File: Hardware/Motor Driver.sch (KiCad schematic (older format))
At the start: 9 parts, among them U5 DRV8874

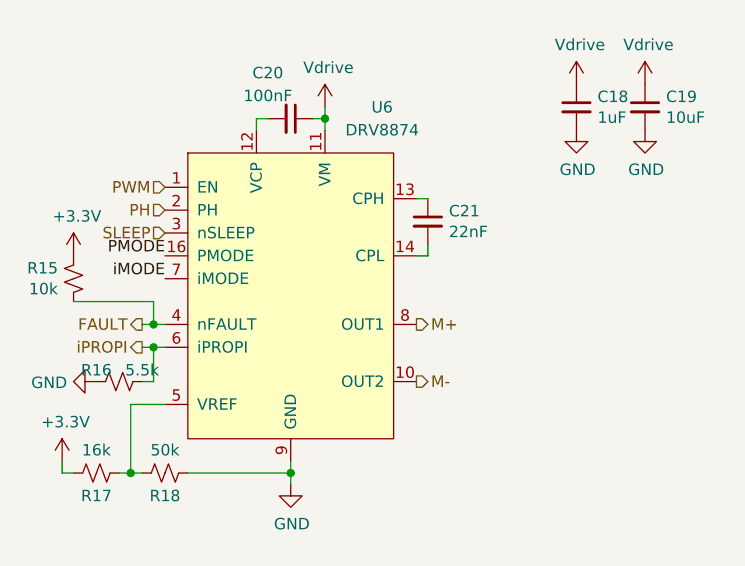
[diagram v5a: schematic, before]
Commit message: Replaced ESP-WROOM-32D with ESP32-CAM
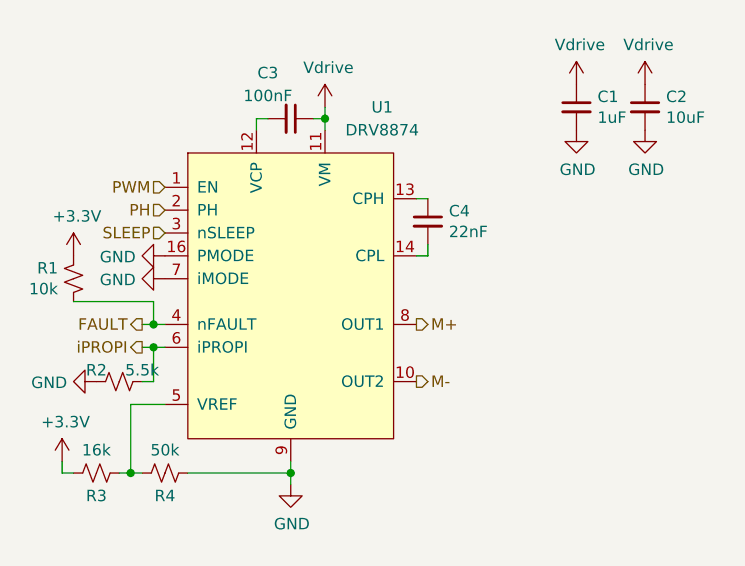
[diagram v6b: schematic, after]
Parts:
- renumbered C14 to C1, C15 to C2, C16 to C3, C17 to C4, R11 to R1, R12 to R2, R13 to R3, R14 to R4, U5 to U1
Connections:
- net PMODE is gone; now on net GND: U1.16 (PMODE)
- net iMODE is gone; now on net GND: U1.7 (iMODE)
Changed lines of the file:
@@
 P 5850 4500
 AR Path="/5FF172EF" Ref="#PWR?"  Part="1"
-AR Path="/5FF00151/5FF172EF" Ref="#PWR027"  Part="1"
-AR Path="/5FF2CF13/5FF172EF" Ref="#PWR036"  Part="1"
-F 0 "#PWR036" H 5850 4250 50  0001 C CNN
+AR Path="/5FF00151/5FF172EF" Ref="#PWR014"  Part="1"
+AR Path="/5FF2CF13/5FF172EF" Ref="#PWR025"  Part="1"
+F 0 "#PWR025" H 5850 4250 50  0001 C CNN
 F 1 "GND" H 5855 4327 50  0000 C CNN
 F 2 "" H 5850 4500 50  0001 C CNN
@@
 AR Path="/5EA2026E/5FF2BF81" Ref="C?"  Part="1"
 AR Path="/5FF2BF81" Ref="C?"  Part="1"
-AR Path="/5FF00151/5FF2BF81" Ref="C17"  Part="1"
-AR Path="/5FF2CF13/5FF2BF81" Ref="C21"  Part="1"
-F 0 "C21" H 6542 3396 50  0000 L CNN
+AR Path="/5FF00151/5FF2BF81" Ref="C4"  Part="1"
+AR Path="/5FF2CF13/5FF2BF81" Ref="C8"  Part="1"
+F 0 "C4" H 6542 3396 50  0000 L CNN
 F 1 "22nF" H 6542 3305 50  0000 L CNN
 F 2 "Resistor_SMD:R_0603_1608Metric" H 6450 3350 50  0001 C CNN
@@
 P 4850 4400
 AR Path="/5FF2D4A0" Ref="#PWR?"  Part="1"
-AR Path="/5FF00151/5FF2D4A0" Ref="#PWR026"  Part="1"
-AR Path="/5FF2CF13/5FF2D4A0" Ref="#PWR035"  Part="1"
-F 0 "#PWR035" H 4850 4250 50  0001 C CNN
+AR Path="/5FF00151/5FF2D4A0" Ref="#PWR013"  Part="1"
+AR Path="/5FF2CF13/5FF2D4A0" Ref="#PWR024"  Part="1"
+F 0 "#PWR024" H 4850 4250 50  0001 C CNN
 F 1 "+3.3V" H 4865 4573 50  0000 C CNN
 F 2 "" H 4850 4400 50  0001 C CNN
@@
 P 5000 4450
 AR Path="/5FF172DB" Ref="R?"  Part="1"
-AR Path="/5FF00151/5FF172DB" Ref="R13"  Part="1"
-AR Path="/5FF2CF13/5FF172DB" Ref="R17"  Part="1"
-F 0 "R17" V 5100 4450 50  0000 C CNN
+AR Path="/5FF00151/5FF172DB" Ref="R3"  Part="1"
+AR Path="/5FF2CF13/5FF172DB" Ref="R7"  Part="1"
+F 0 "R3" V 5100 4450 50  0000 C CNN
 F 1 "16k" V 4900 4450 50  0000 C CNN
 F 2 "Resistor_SMD:R_0603_1608Metric" H 5000 4450 50  0001 C CNN
@@
 P 7400 2750
 AR Path="/5FF2D498" Ref="#PWR?"  Part="1"
-AR Path="/5FF00151/5FF2D498" Ref="#PWR020"  Part="1"
-AR Path="/5FF2CF13/5FF2D498" Ref="#PWR029"  Part="1"
-F 0 "#PWR029" H 7200 2600 50  0001 C CNN
+AR Path="/5FF00151/5FF2D498" Ref="#PWR05"  Part="1"
+AR Path="/5FF2CF13/5FF2D498" Ref="#PWR016"  Part="1"
+F 0 "#PWR016" H 7200 2600 50  0001 C CNN
 F 1 "Vdrive" H 7415 2923 50  0000 C CNN
 F 2 "" H 7400 2750 50  0001 C CNN
@@
 P 7100 2750
 AR Path="/5FF172EC" Ref="#PWR?"  Part="1"
-AR Path="/5FF00151/5FF172EC" Ref="#PWR019"  Part="1"
-AR Path="/5FF2CF13/5FF172EC" Ref="#PWR028"  Part="1"
-F 0 "#PWR028" H 6900 2600 50  0001 C CNN
+AR Path="/5FF00151/5FF172EC" Ref="#PWR04"  Part="1"
+AR Path="/5FF2CF13/5FF172EC" Ref="#PWR015"  Part="1"
+F 0 "#PWR015" H 6900 2600 50  0001 C CNN
 F 1 "Vdrive" H 7115 2923 50  0000 C CNN
 F 2 "" H 7100 2750 50  0001 C CNN
@@
 P 7100 2850
 AR Path="/5FF172D6" Ref="C?"  Part="1"
-AR Path="/5FF00151/5FF172D6" Ref="C14"  Part="1"
-AR Path="/5FF2CF13/5FF172D6" Ref="C18"  Part="1"
-F 0 "C18" H 7192 2896 50  0000 L CNN
+AR Path="/5FF00151/5FF172D6" Ref="C1"  Part="1"
+AR Path="/5FF2CF13/5FF172D6" Ref="C5"  Part="1"
+F 0 "C1" H 7192 2896 50  0000 L CNN
 F 1 "1uF" H 7192 2805 50  0000 L CNN
 F 2 "Resistor_SMD:R_0603_1608Metric" H 7100 2850 50  0001 C CNN
@@
 P 7100 2950
 AR Path="/5FF2BF19" Ref="#PWR?"  Part="1"
-AR Path="/5FF00151/5FF2BF19" Ref="#PWR022"  Part="1"
-AR Path="/5FF2CF13/5FF2BF19" Ref="#PWR031"  Part="1"
-F 0 "#PWR031" H 7100 2700 50  0001 C CNN
+AR Path="/5FF00151/5FF2BF19" Ref="#PWR07"  Part="1"
+AR Path="/5FF2CF13/5FF2BF19" Ref="#PWR018"  Part="1"
+F 0 "#PWR018" H 7100 2700 50  0001 C CNN
 F 1 "GND" H 7105 2777 50  0000 C CNN
 F 2 "" H 7100 2950 50  0001 C CNN
@@
 P 7400 2950
 AR Path="/5FF2D48C" Ref="#PWR?"  Part="1"
-AR Path="/5FF00151/5FF2D48C" Ref="#PWR023"  Part="1"
-AR Path="/5FF2CF13/5FF2D48C" Ref="#PWR032"  Part="1"
-F 0 "#PWR032" H 7400 2700 50  0001 C CNN
+AR Path="/5FF00151/5FF2D48C" Ref="#PWR08"  Part="1"
+AR Path="/5FF2CF13/5FF2D48C" Ref="#PWR019"  Part="1"
+F 0 "#PWR019" H 7400 2700 50  0001 C CNN
 F 1 "GND" H 7405 2777 50  0000 C CNN
 F 2 "" H 7400 2950 50  0001 C CNN
@@
 P 5000 4050
 AR Path="/5FF2D49F" Ref="#PWR?"  Part="1"
-AR Path="/5FF00151/5FF2D49F" Ref="#PWR025"  Part="1"
-AR Path="/5FF2CF13/5FF2D49F" Ref="#PWR034"  Part="1"
-F 0 "#PWR034" H 5000 3800 50  0001 C CNN
+AR Path="/5FF00151/5FF2D49F" Ref="#PWR012"  Part="1"
+AR Path="/5FF2CF13/5FF2D49F" Ref="#PWR023"  Part="1"
+F 0 "#PWR023" H 5000 3800 50  0001 C CNN
 F 1 "GND" V 5005 3922 50  0000 R CNN
 F 2 "" H 5000 4050 50  0001 C CNN
@@
 AR Path="/5EA2026E/5FF2D494" Ref="R?"  Part="1"
 AR Path="/5FF2D494" Ref="R?"  Part="1"
-AR Path="/5FF00151/5FF2D494" Ref="R11"  Part="1"
-AR Path="/5FF2CF13/5FF2D494" Ref="R15"  Part="1"
-F 0 "R15" H 4968 3646 50  0000 L CNN
+AR Path="/5FF00151/5FF2D494" Ref="R1"  Part="1"
+AR Path="/5FF2CF13/5FF2D494" Ref="R5"  Part="1"
+F 0 "R1" H 4968 3646 50  0000 L CNN
 F 1 "10k" H 4968 3555 50  0000 L CNN
 F 2 "Resistor_SMD:R_0603_1608Metric" H 4900 3600 50  0001 C CNN
@@
 Text HLabel 5300 3400 0    50   Input ~ 0
 SLEEP
-Text Label 5300 3500 2    50   ~ 0
-PMODE
-Text Label 5300 3600 2    50   ~ 0
-iMODE
 Text HLabel 5200 3800 0    50   Output ~ 0
 FAULT
@@
 P 7400 2850
 AR Path="/5FF2D490" Ref="C?"  Part="1"
-AR Path="/5FF00151/5FF2D490" Ref="C15"  Part="1"
-AR Path="/5FF2CF13/5FF2D490" Ref="C19"  Part="1"
-F 0 "C19" H 7492 2896 50  0000 L CNN
+AR Path="/5FF00151/5FF2D490" Ref="C2"  Part="1"
+AR Path="/5FF2CF13/5FF2D490" Ref="C6"  Part="1"
+F 0 "C2" H 7492 2896 50  0000 L CNN
 F 1 "10uF" H 7492 2805 50  0000 L CNN
 F 2 "Capacitor_SMD:C_2220_5650Metric" H 7400 2850 50  0001 C CNN
@@
 P 4900 3500
 AR Path="/5FF172E1" Ref="#PWR?"  Part="1"
-AR Path="/5FF00151/5FF172E1" Ref="#PWR024"  Part="1"
-AR Path="/5FF2CF13/5FF172E1" Ref="#PWR033"  Part="1"
-F 0 "#PWR033" H 4900 3350 50  0001 C CNN
+AR Path="/5FF00151/5FF172E1" Ref="#PWR09"  Part="1"
+AR Path="/5FF2CF13/5FF172E1" Ref="#PWR020"  Part="1"
+F 0 "#PWR020" H 4900 3350 50  0001 C CNN
 F 1 "+3.3V" H 4915 3673 50  0000 C CNN
 F 2 "" H 4900 3500 50  0001 C CNN
@@
 P 5100 4050
 AR Path="/5FF2D49E" Ref="R?"  Part="1"
-AR Path="/5FF00151/5FF2D49E" Ref="R12"  Part="1"
-AR Path="/5FF2CF13/5FF2D49E" Ref="R16"  Part="1"
-F 0 "R16" V 5050 3950 50  0000 C CNN
+AR Path="/5FF00151/5FF2D49E" Ref="R2"  Part="1"
+AR Path="/5FF2CF13/5FF2D49E" Ref="R6"  Part="1"
+F 0 "R2" V 5050 3950 50  0000 C CNN
 F 1 "5.5k" V 5050 4150 50  0000 C CNN
 F 2 "Resistor_SMD:R_0603_1608Metric" H 5100 4050 50  0001 C CNN
@@
 P 5300 4450
 AR Path="/5FF172DD" Ref="R?"  Part="1"
-AR Path="/5FF00151/5FF172DD" Ref="R14"  Part="1"
-AR Path="/5FF2CF13/5FF172DD" Ref="R18"  Part="1"
-F 0 "R18" V 5400 4450 50  0000 C CNN
+AR Path="/5FF00151/5FF172DD" Ref="R4"  Part="1"
+AR Path="/5FF2CF13/5FF172DD" Ref="R8"  Part="1"
+F 0 "R4" V 5400 4450 50  0000 C CNN
 F 1 "50k" V 5200 4450 50  0000 C CNN
 F 2 "Resistor_SMD:R_0603_1608Metric" H 5300 4450 50  0001 C CNN
@@
 P 6000 2850
 AR Path="/5FF2D4A1" Ref="#PWR?"  Part="1"
-AR Path="/5FF00151/5FF2D4A1" Ref="#PWR021"  Part="1"
-AR Path="/5FF2CF13/5FF2D4A1" Ref="#PWR030"  Part="1"
-F 0 "#PWR030" H 5800 2700 50  0001 C CNN
+AR Path="/5FF00151/5FF2D4A1" Ref="#PWR06"  Part="1"
+AR Path="/5FF2CF13/5FF2D4A1" Ref="#PWR017"  Part="1"
+F 0 "#PWR017" H 5800 2700 50  0001 C CNN
 F 1 "Vdrive" H 6015 3023 50  0000 C CNN
 F 2 "" H 6000 2850 50  0001 C CNN
@@
 P 5850 2900
 AR Path="/5FF2D4A2" Ref="C?"  Part="1"
-AR Path="/5FF00151/5FF2D4A2" Ref="C16"  Part="1"
-AR Path="/5FF2CF13/5FF2D4A2" Ref="C20"  Part="1"
-F 0 "C20" V 5650 2800 50  0000 C CNN
+AR Path="/5FF00151/5FF2D4A2" Ref="C3"  Part="1"
+AR Path="/5FF2CF13/5FF2D4A2" Ref="C7"  Part="1"
+F 0 "C3" V 5650 2800 50  0000 C CNN
 F 1 "100nF" V 5750 2800 50  0000 C CNN
 F 2 "Resistor_SMD:R_0603_1608Metric" H 5850 2900 50  0001 C CNN
@@
 P 5850 3050
 AR Path="/5FF172F1" Ref="U?"  Part="1"
-AR Path="/5FF00151/5FF172F1" Ref="U5"  Part="1"
-AR Path="/5FF2CF13/5FF172F1" Ref="U6"  Part="1"
-F 0 "U6" H 6250 3250 50  0000 C CNN
+AR Path="/5FF00151/5FF172F1" Ref="U1"  Part="1"
+AR Path="/5FF2CF13/5FF172F1" Ref="U2"  Part="1"
+F 0 "U1" H 6250 3250 50  0000 C CNN
 F 1 "DRV8874" H 6250 3150 50  0000 C CNN
 F 2 "Package_SO:HTSSOP-16-1EP_4.4x5mm_P0.65mm_EP3.4x5mm_Mask3x3mm_ThermalVias" H 6200 3200 50  0001 C CNN
@@
 	1    0    0    -1
 $EndComp
+$Comp
+L power:GND #PWR010
+U 1 1 5FF4A672
+P 5300 3500
+AR Path="/5FF00151/5FF4A672" Ref="#PWR010"  Part="1"
+AR Path="/5FF2CF13/5FF4A672" Ref="#PWR021"  Part="1"
+F 0 "#PWR021" H 5300 3250 50  0001 C CNN
+F 1 "GND" V 5305 3372 50  0000 R CNN
+F 2 "" H 5300 3500 50  0001 C CNN
+F 3 "" H 5300 3500 50  0001 C CNN
+	1    5300 3500
+	0    1    1    0
+$EndComp
+$Comp
+L power:GND #PWR011
+U 1 1 5FF4ADD9
+P 5300 3600
+AR Path="/5FF00151/5FF4ADD9" Ref="#PWR011"  Part="1"
+AR Path="/5FF2CF13/5FF4ADD9" Ref="#PWR022"  Part="1"
+F 0 "#PWR022" H 5300 3350 50  0001 C CNN
+F 1 "GND" V 5305 3472 50  0000 R CNN
+F 2 "" H 5300 3600 50  0001 C CNN
+F 3 "" H 5300 3600 50  0001 C CNN
+	1    5300 3600
+	0    1    1    0
+$EndComp
 $EndSCHEMATC

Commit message: Schematic updated, USB comms circuit added
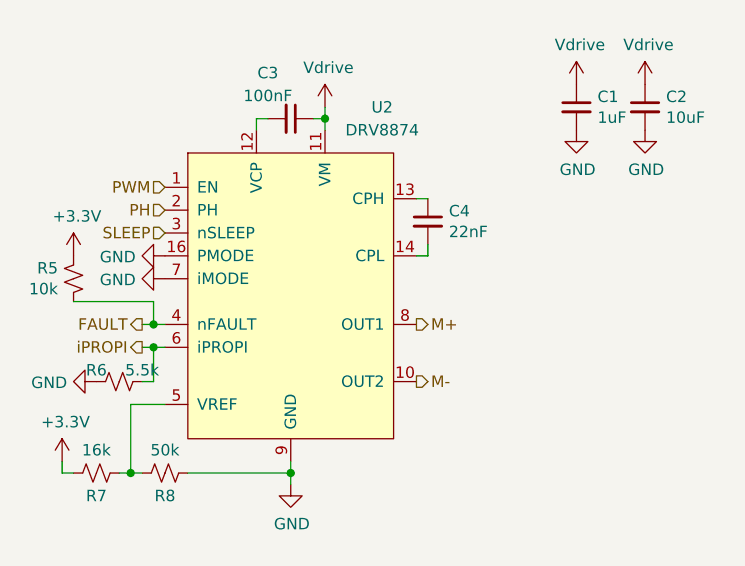
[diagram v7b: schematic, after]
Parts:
- C1, C3, C4: footprint Resistor_SMD:R_0603_1608Metric -> Capacitor_SMD:C_0805_2012Metric
- R5: renamed from R1; footprint Resistor_SMD:R_0603_1608Metric -> Resistor_SMD:R_0805_2012Metric
- R6: renamed from R2; footprint Resistor_SMD:R_0603_1608Metric -> Resistor_SMD:R_0805_2012Metric
- R7: renamed from R3; footprint Resistor_SMD:R_0603_1608Metric -> Resistor_SMD:R_0805_2012Metric
- R8: renamed from R4; footprint Resistor_SMD:R_0603_1608Metric -> Resistor_SMD:R_0805_2012Metric
- renumbered U1 to U2
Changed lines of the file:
@@
 $Descr A4 11693 8268
 encoding utf-8
-Sheet 2 9
+Sheet 2 11
 Title ""
 Date ""
@@
 P 5850 4500
 AR Path="/5FF172EF" Ref="#PWR?"  Part="1"
-AR Path="/5FF00151/5FF172EF" Ref="#PWR014"  Part="1"
-AR Path="/5FF2CF13/5FF172EF" Ref="#PWR025"  Part="1"
-F 0 "#PWR025" H 5850 4250 50  0001 C CNN
+AR Path="/5FF00151/5FF172EF" Ref="#PWR018"  Part="1"
+AR Path="/5FF2CF13/5FF172EF" Ref="#PWR029"  Part="1"
+F 0 "#PWR029" H 5850 4250 50  0001 C CNN
 F 1 "GND" H 5855 4327 50  0000 C CNN
 F 2 "" H 5850 4500 50  0001 C CNN
@@
 F 0 "C4" H 6542 3396 50  0000 L CNN
 F 1 "22nF" H 6542 3305 50  0000 L CNN
-F 2 "Resistor_SMD:R_0603_1608Metric" H 6450 3350 50  0001 C CNN
+F 2 "Capacitor_SMD:C_0805_2012Metric" H 6450 3350 50  0001 C CNN
 F 3 "https://lcsc.com/product-detail/Multilayer-Ceramic-Capacitors-MLCC-SMD-SMT_100nF-104-10-50V_C49678.html/?href=jlc-SMT" H 6450 3350 50  0001 C CNN
 	1    6450 3350
@@
 P 4850 4400
 AR Path="/5FF2D4A0" Ref="#PWR?"  Part="1"
-AR Path="/5FF00151/5FF2D4A0" Ref="#PWR013"  Part="1"
-AR Path="/5FF2CF13/5FF2D4A0" Ref="#PWR024"  Part="1"
-F 0 "#PWR024" H 4850 4250 50  0001 C CNN
+AR Path="/5FF00151/5FF2D4A0" Ref="#PWR017"  Part="1"
+AR Path="/5FF2CF13/5FF2D4A0" Ref="#PWR028"  Part="1"
+F 0 "#PWR028" H 4850 4250 50  0001 C CNN
 F 1 "+3.3V" H 4865 4573 50  0000 C CNN
 F 2 "" H 4850 4400 50  0001 C CNN
@@
 P 5000 4450
 AR Path="/5FF172DB" Ref="R?"  Part="1"
-AR Path="/5FF00151/5FF172DB" Ref="R3"  Part="1"
-AR Path="/5FF2CF13/5FF172DB" Ref="R7"  Part="1"
-F 0 "R3" V 5100 4450 50  0000 C CNN
+AR Path="/5FF00151/5FF172DB" Ref="R7"  Part="1"
+AR Path="/5FF2CF13/5FF172DB" Ref="R11"  Part="1"
+F 0 "R7" V 5100 4450 50  0000 C CNN
 F 1 "16k" V 4900 4450 50  0000 C CNN
-F 2 "Resistor_SMD:R_0603_1608Metric" H 5000 4450 50  0001 C CNN
+F 2 "Resistor_SMD:R_0805_2012Metric" H 5000 4450 50  0001 C CNN
 F 3 "~" H 5000 4450 50  0001 C CNN
 	1    5000 4450
@@
 P 7400 2750
 AR Path="/5FF2D498" Ref="#PWR?"  Part="1"
-AR Path="/5FF00151/5FF2D498" Ref="#PWR05"  Part="1"
-AR Path="/5FF2CF13/5FF2D498" Ref="#PWR016"  Part="1"
-F 0 "#PWR016" H 7200 2600 50  0001 C CNN
+AR Path="/5FF00151/5FF2D498" Ref="#PWR09"  Part="1"
+AR Path="/5FF2CF13/5FF2D498" Ref="#PWR020"  Part="1"
+F 0 "#PWR020" H 7200 2600 50  0001 C CNN
 F 1 "Vdrive" H 7415 2923 50  0000 C CNN
 F 2 "" H 7400 2750 50  0001 C CNN
@@
 P 7100 2750
 AR Path="/5FF172EC" Ref="#PWR?"  Part="1"
-AR Path="/5FF00151/5FF172EC" Ref="#PWR04"  Part="1"
-AR Path="/5FF2CF13/5FF172EC" Ref="#PWR015"  Part="1"
-F 0 "#PWR015" H 6900 2600 50  0001 C CNN
+AR Path="/5FF00151/5FF172EC" Ref="#PWR08"  Part="1"
+AR Path="/5FF2CF13/5FF172EC" Ref="#PWR019"  Part="1"
+F 0 "#PWR019" H 6900 2600 50  0001 C CNN
 F 1 "Vdrive" H 7115 2923 50  0000 C CNN
 F 2 "" H 7100 2750 50  0001 C CNN
@@
 F 0 "C1" H 7192 2896 50  0000 L CNN
 F 1 "1uF" H 7192 2805 50  0000 L CNN
-F 2 "Resistor_SMD:R_0603_1608Metric" H 7100 2850 50  0001 C CNN
+F 2 "Capacitor_SMD:C_0805_2012Metric" H 7100 2850 50  0001 C CNN
 F 3 "~" H 7100 2850 50  0001 C CNN
 	1    7100 2850
@@
 P 7100 2950
 AR Path="/5FF2BF19" Ref="#PWR?"  Part="1"
-AR Path="/5FF00151/5FF2BF19" Ref="#PWR07"  Part="1"
-AR Path="/5FF2CF13/5FF2BF19" Ref="#PWR018"  Part="1"
-F 0 "#PWR018" H 7100 2700 50  0001 C CNN
+AR Path="/5FF00151/5FF2BF19" Ref="#PWR011"  Part="1"
+AR Path="/5FF2CF13/5FF2BF19" Ref="#PWR022"  Part="1"
+F 0 "#PWR022" H 7100 2700 50  0001 C CNN
 F 1 "GND" H 7105 2777 50  0000 C CNN
 F 2 "" H 7100 2950 50  0001 C CNN
@@
 P 7400 2950
 AR Path="/5FF2D48C" Ref="#PWR?"  Part="1"
-AR Path="/5FF00151/5FF2D48C" Ref="#PWR08"  Part="1"
-AR Path="/5FF2CF13/5FF2D48C" Ref="#PWR019"  Part="1"
-F 0 "#PWR019" H 7400 2700 50  0001 C CNN
+AR Path="/5FF00151/5FF2D48C" Ref="#PWR012"  Part="1"
+AR Path="/5FF2CF13/5FF2D48C" Ref="#PWR023"  Part="1"
+F 0 "#PWR023" H 7400 2700 50  0001 C CNN
 F 1 "GND" H 7405 2777 50  0000 C CNN
 F 2 "" H 7400 2950 50  0001 C CNN
@@
 P 5000 4050
 AR Path="/5FF2D49F" Ref="#PWR?"  Part="1"
-AR Path="/5FF00151/5FF2D49F" Ref="#PWR012"  Part="1"
-AR Path="/5FF2CF13/5FF2D49F" Ref="#PWR023"  Part="1"
-F 0 "#PWR023" H 5000 3800 50  0001 C CNN
+AR Path="/5FF00151/5FF2D49F" Ref="#PWR016"  Part="1"
+AR Path="/5FF2CF13/5FF2D49F" Ref="#PWR027"  Part="1"
+F 0 "#PWR027" H 5000 3800 50  0001 C CNN
 F 1 "GND" V 5005 3922 50  0000 R CNN
 F 2 "" H 5000 4050 50  0001 C CNN
@@
 AR Path="/5EA2026E/5FF2D494" Ref="R?"  Part="1"
 AR Path="/5FF2D494" Ref="R?"  Part="1"
-AR Path="/5FF00151/5FF2D494" Ref="R1"  Part="1"
-AR Path="/5FF2CF13/5FF2D494" Ref="R5"  Part="1"
-F 0 "R1" H 4968 3646 50  0000 L CNN
+AR Path="/5FF00151/5FF2D494" Ref="R5"  Part="1"
+AR Path="/5FF2CF13/5FF2D494" Ref="R9"  Part="1"
+F 0 "R5" H 4968 3646 50  0000 L CNN
 F 1 "10k" H 4968 3555 50  0000 L CNN
-F 2 "Resistor_SMD:R_0603_1608Metric" H 4900 3600 50  0001 C CNN
+F 2 "Resistor_SMD:R_0805_2012Metric" H 4900 3600 50  0001 C CNN
 F 3 "https://lcsc.com/product-detail/Chip-Resistor-Surface-Mount_Uniroyal-Elec-0805W8F1002T5E_C17414.html/?href=jlc-SMT" H 4900 3600 50  0001 C CNN
 	1    4900 3600
@@
 P 4900 3500
 AR Path="/5FF172E1" Ref="#PWR?"  Part="1"
-AR Path="/5FF00151/5FF172E1" Ref="#PWR09"  Part="1"
-AR Path="/5FF2CF13/5FF172E1" Ref="#PWR020"  Part="1"
-F 0 "#PWR020" H 4900 3350 50  0001 C CNN
+AR Path="/5FF00151/5FF172E1" Ref="#PWR013"  Part="1"
+AR Path="/5FF2CF13/5FF172E1" Ref="#PWR024"  Part="1"
+F 0 "#PWR024" H 4900 3350 50  0001 C CNN
 F 1 "+3.3V" H 4915 3673 50  0000 C CNN
 F 2 "" H 4900 3500 50  0001 C CNN
@@
 P 5100 4050
 AR Path="/5FF2D49E" Ref="R?"  Part="1"
-AR Path="/5FF00151/5FF2D49E" Ref="R2"  Part="1"
-AR Path="/5FF2CF13/5FF2D49E" Ref="R6"  Part="1"
-F 0 "R2" V 5050 3950 50  0000 C CNN
+AR Path="/5FF00151/5FF2D49E" Ref="R6"  Part="1"
+AR Path="/5FF2CF13/5FF2D49E" Ref="R10"  Part="1"
+F 0 "R6" V 5050 3950 50  0000 C CNN
 F 1 "5.5k" V 5050 4150 50  0000 C CNN
-F 2 "Resistor_SMD:R_0603_1608Metric" H 5100 4050 50  0001 C CNN
+F 2 "Resistor_SMD:R_0805_2012Metric" H 5100 4050 50  0001 C CNN
 F 3 "~" H 5100 4050 50  0001 C CNN
 	1    5100 4050
@@
 P 5300 4450
 AR Path="/5FF172DD" Ref="R?"  Part="1"
-AR Path="/5FF00151/5FF172DD" Ref="R4"  Part="1"
-AR Path="/5FF2CF13/5FF172DD" Ref="R8"  Part="1"
-F 0 "R4" V 5400 4450 50  0000 C CNN
+AR Path="/5FF00151/5FF172DD" Ref="R8"  Part="1"
+AR Path="/5FF2CF13/5FF172DD" Ref="R12"  Part="1"
+F 0 "R8" V 5400 4450 50  0000 C CNN
 F 1 "50k" V 5200 4450 50  0000 C CNN
-F 2 "Resistor_SMD:R_0603_1608Metric" H 5300 4450 50  0001 C CNN
+F 2 "Resistor_SMD:R_0805_2012Metric" H 5300 4450 50  0001 C CNN
 F 3 "~" H 5300 4450 50  0001 C CNN
 	1    5300 4450
@@
 P 6000 2850
 AR Path="/5FF2D4A1" Ref="#PWR?"  Part="1"
-AR Path="/5FF00151/5FF2D4A1" Ref="#PWR06"  Part="1"
-AR Path="/5FF2CF13/5FF2D4A1" Ref="#PWR017"  Part="1"
-F 0 "#PWR017" H 5800 2700 50  0001 C CNN
+AR Path="/5FF00151/5FF2D4A1" Ref="#PWR010"  Part="1"
+AR Path="/5FF2CF13/5FF2D4A1" Ref="#PWR021"  Part="1"
+F 0 "#PWR021" H 5800 2700 50  0001 C CNN
 F 1 "Vdrive" H 6015 3023 50  0000 C CNN
 F 2 "" H 6000 2850 50  0001 C CNN
@@
 F 0 "C3" V 5650 2800 50  0000 C CNN
 F 1 "100nF" V 5750 2800 50  0000 C CNN
-F 2 "Resistor_SMD:R_0603_1608Metric" H 5850 2900 50  0001 C CNN
+F 2 "Capacitor_SMD:C_0805_2012Metric" H 5850 2900 50  0001 C CNN
 F 3 "~" H 5850 2900 50  0001 C CNN
 	1    5850 2900
@@
 P 5850 3050
 AR Path="/5FF172F1" Ref="U?"  Part="1"
-AR Path="/5FF00151/5FF172F1" Ref="U1"  Part="1"
-AR Path="/5FF2CF13/5FF172F1" Ref="U2"  Part="1"
-F 0 "U1" H 6250 3250 50  0000 C CNN
+AR Path="/5FF00151/5FF172F1" Ref="U2"  Part="1"
+AR Path="/5FF2CF13/5FF172F1" Ref="U3"  Part="1"
+F 0 "U2" H 6250 3250 50  0000 C CNN
 F 1 "DRV8874" H 6250 3150 50  0000 C CNN
 F 2 "Package_SO:HTSSOP-16-1EP_4.4x5mm_P0.65mm_EP3.4x5mm_Mask3x3mm_ThermalVias" H 6200 3200 50  0001 C CNN
@@
 $EndComp
 $Comp
-L power:GND #PWR010
+L power:GND #PWR014
 U 1 1 5FF4A672
 P 5300 3500
-AR Path="/5FF00151/5FF4A672" Ref="#PWR010"  Part="1"
-AR Path="/5FF2CF13/5FF4A672" Ref="#PWR021"  Part="1"
-F 0 "#PWR021" H 5300 3250 50  0001 C CNN
+AR Path="/5FF00151/5FF4A672" Ref="#PWR014"  Part="1"
+AR Path="/5FF2CF13/5FF4A672" Ref="#PWR025"  Part="1"
+F 0 "#PWR025" H 5300 3250 50  0001 C CNN
 F 1 "GND" V 5305 3372 50  0000 R CNN
 F 2 "" H 5300 3500 50  0001 C CNN
@@
 $EndComp
 $Comp
-L power:GND #PWR011
+L power:GND #PWR015
 U 1 1 5FF4ADD9
 P 5300 3600
-AR Path="/5FF00151/5FF4ADD9" Ref="#PWR011"  Part="1"
-AR Path="/5FF2CF13/5FF4ADD9" Ref="#PWR022"  Part="1"
-F 0 "#PWR022" H 5300 3350 50  0001 C CNN
+AR Path="/5FF00151/5FF4ADD9" Ref="#PWR015"  Part="1"
+AR Path="/5FF2CF13/5FF4ADD9" Ref="#PWR026"  Part="1"
+F 0 "#PWR026" H 5300 3350 50  0001 C CNN
 F 1 "GND" V 5305 3472 50  0000 R CNN
 F 2 "" H 5300 3600 50  0001 C CNN
